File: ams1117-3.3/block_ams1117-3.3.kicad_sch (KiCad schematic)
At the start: 9 parts, among them U1 AMS1117-3.3

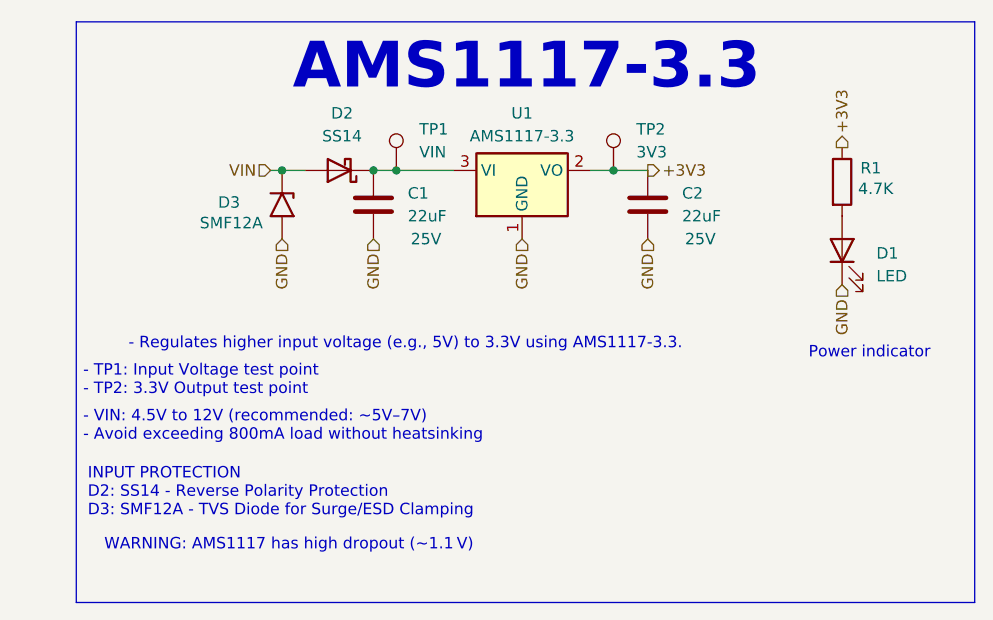
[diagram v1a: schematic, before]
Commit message: finalised AMS1117
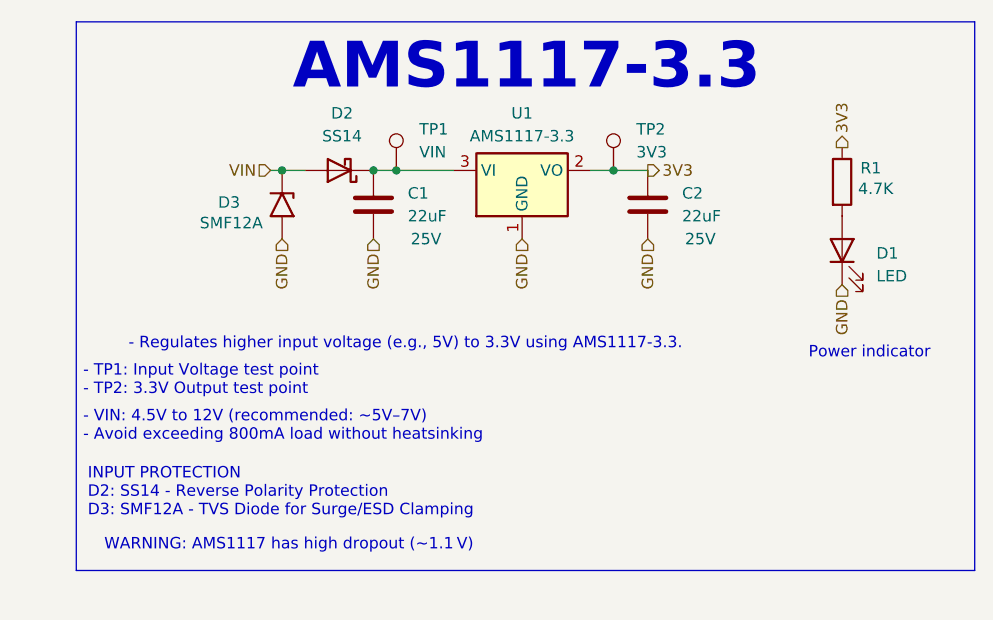
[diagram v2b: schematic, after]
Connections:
- net +3V3 renamed 3V3
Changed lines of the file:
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@@
 	(rectangle
 		(start 87.63 73.66)
-		(end 187.452 138.176)
+		(end 187.452 134.62)
 		(stroke
 			(width 0)
@@
 		)
 	)
-	(hierarchical_label "+3V3"
+	(hierarchical_label "3V3"
 		(shape output)
 		(at 151.13 90.17 0)
@@
 		)
 	)
-	(hierarchical_label "+3V3"
+	(hierarchical_label "3V3"
 		(shape output)
 		(at 172.72 87.63 90)
